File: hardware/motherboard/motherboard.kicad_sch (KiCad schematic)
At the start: 78 parts, among them J1 JST-VH, J2 USB C 2.0, J3 JST-VH, J4 JST-PH, Q1 TSM7P06CP_ROG, Q2 TSM7P06CP_ROG, SW1 Boot, SW10 B, SW11 X, SW12 Y, SW13 Start, SW14 Select, SW2 Reset, SW3 A, SW4 B, SW5 LB, SW6 RB, SW7 X, SW8 Y, SW9 A, U1 ESP32-S3-WROOM-1, U2 TPS75533KTTRG3, U3 TLV75709PDBV

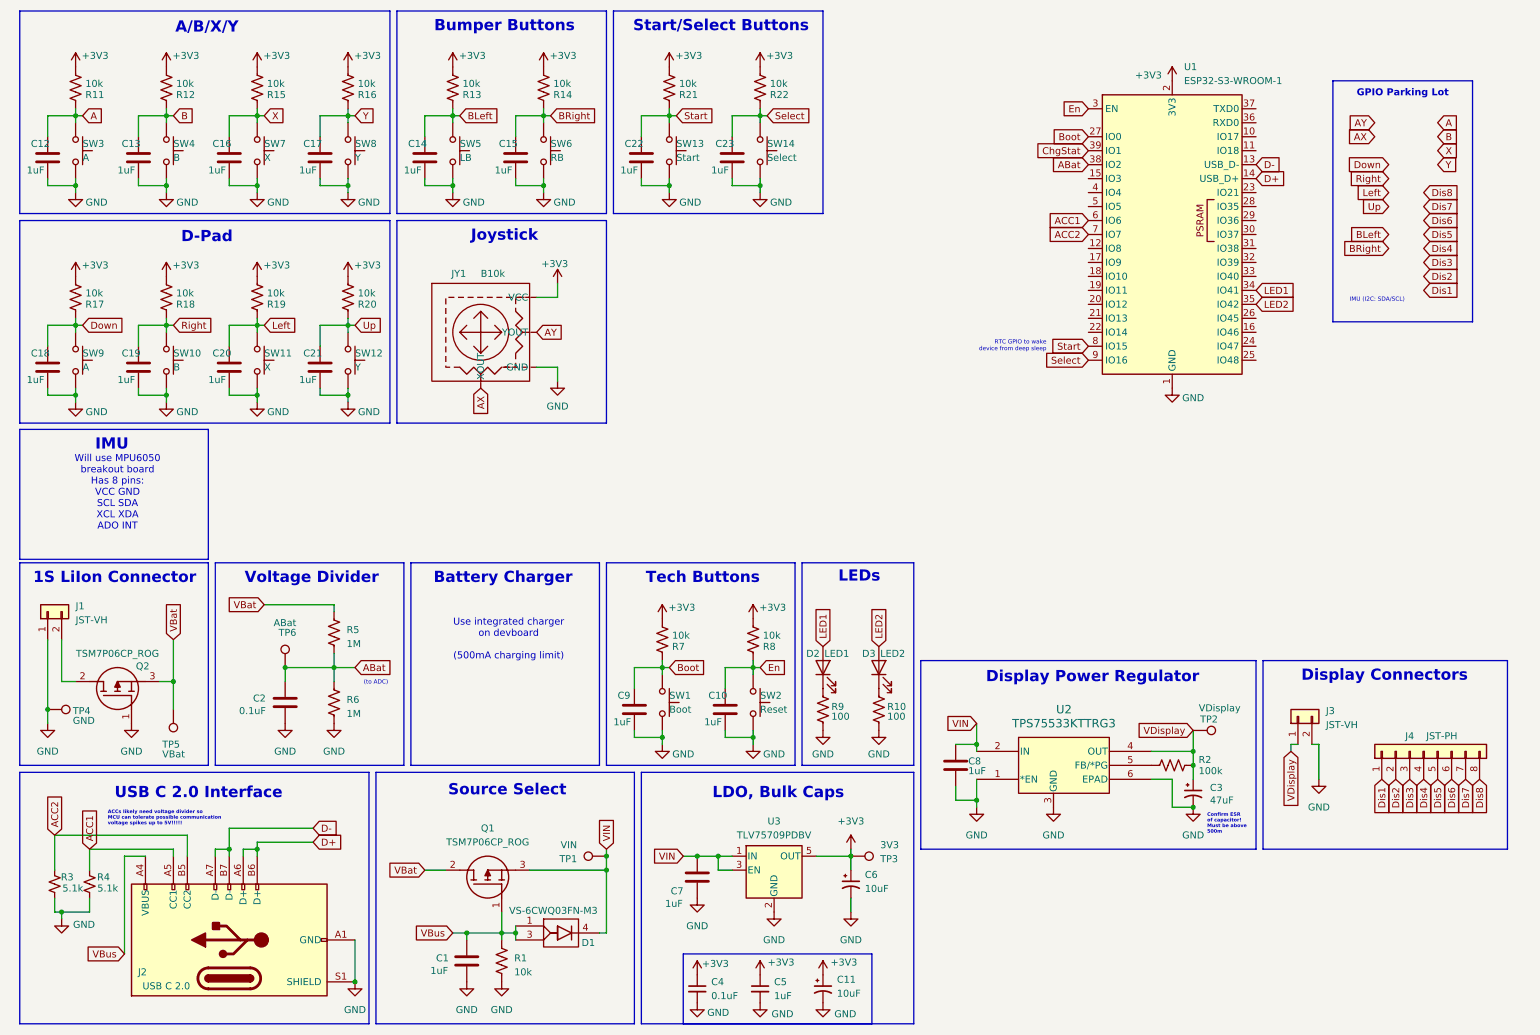
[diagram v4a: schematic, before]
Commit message: Charger, Started GPIO Assignments
Added ESP32 devboard charger circuit and began assigning GPIOs. Provided lots of annotations and justifications for GPIO assignments.
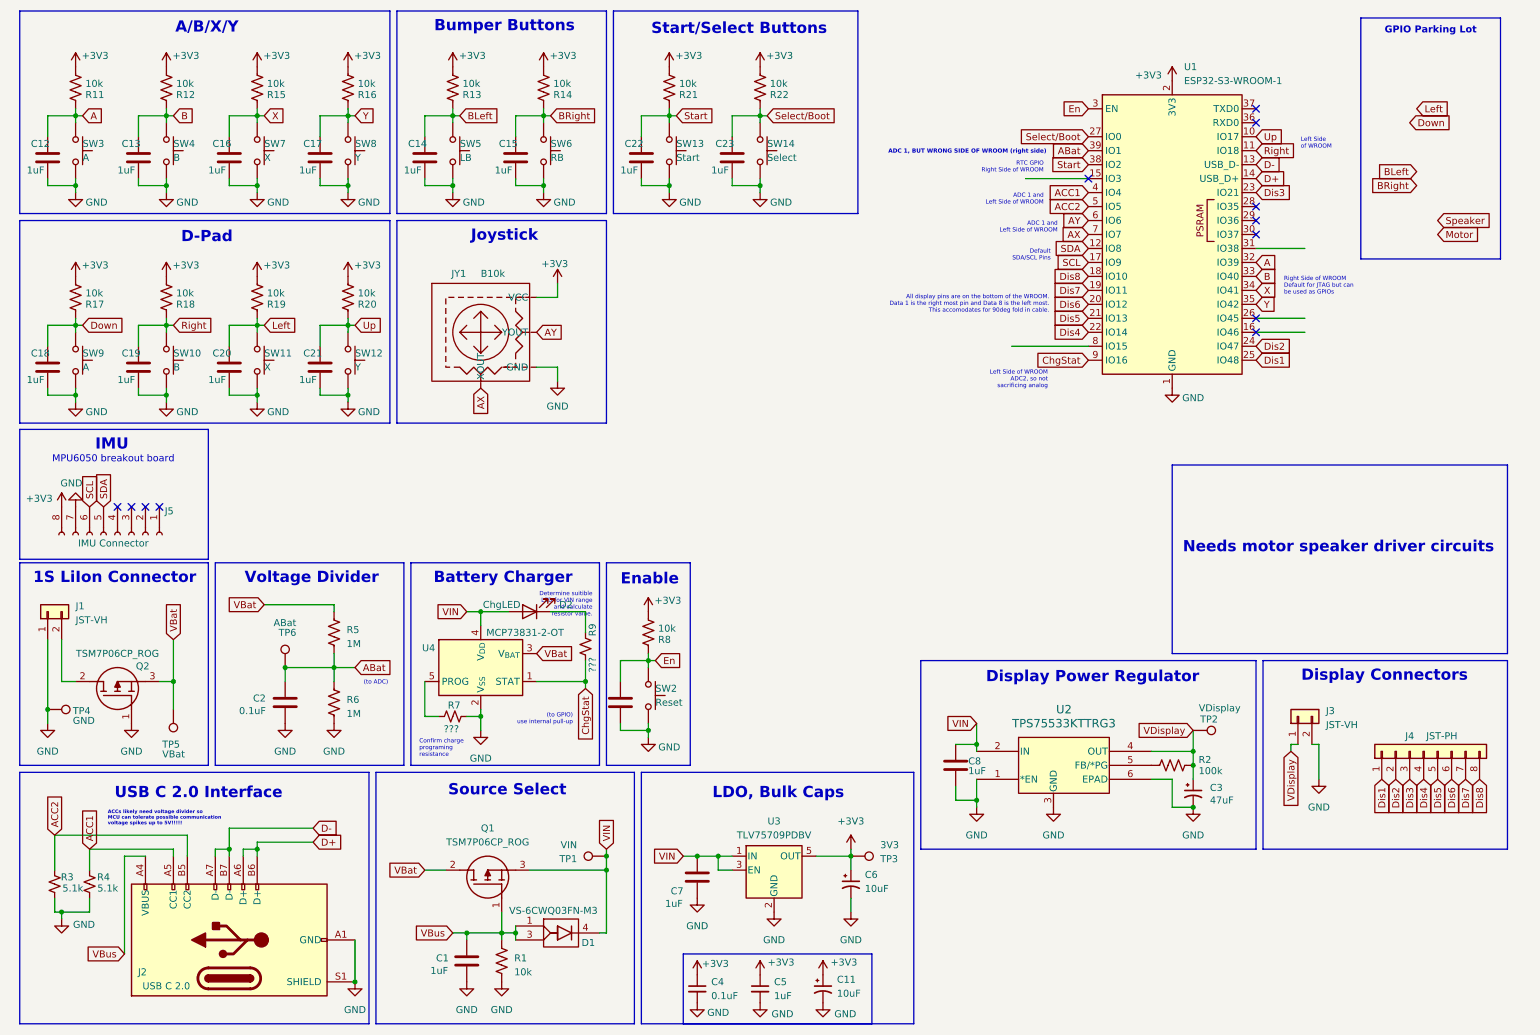
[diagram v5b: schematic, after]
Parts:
- removed C9: 1uF, symbol Device:C
- removed D3: LED2, symbol Device:LED
- removed R10, R9: 100, Resistor_SMD:R_0603_1608Metric, symbol Device:R_US
- removed R7: 10k, Resistor_SMD:R_0603_1608Metric, symbol Device:R_US
- removed SW1: Boot, symbol Switch:SW_Push
- added J5: IMU Connector, symbol Connector:Conn_01x08_Socket
- added R7, R9: ???, symbol Device:R_Small_US
- added U4: MCP73831-2-OT, Package_TO_SOT_SMD:SOT-23-5, symbol Battery_Management:MCP73831-2-OT
- D2: value LED1 -> ChgLED
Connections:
- net LED2 is gone; now on net Y: U1.35 (IO42)
- net +3V3: now also J5.8 (Pin_8)
- net A: now also U1.32 (IO39)
- net ABat: now also U1.39 (IO1); no longer U1.38 (IO2)
- net ACC1: now also U1.4 (IO4); no longer U1.6 (IO6)
- net ACC2: now also U1.5 (IO5); no longer U1.7 (IO7)
- net AX: now also U1.7 (IO7)
- net AY: now also U1.6 (IO6)
- net B: now also U1.33 (IO40)
- net ChgStat: now also U1.9 (IO16), R9.1, U4.1 (STAT); no longer U1.39 (IO1)
- net Dis1: now also U1.25 (IO48)
- net Dis2: now also U1.24 (IO47)
- net Dis3: now also U1.23 (IO21)
- net Dis4: now also U1.22 (IO14)
- net Dis5: now also U1.21 (IO13)
- net Dis6: now also U1.20 (IO12)
- net Dis7: now also U1.19 (IO11)
- net Dis8: now also U1.18 (IO10)
- net GND: now also J5.7 (Pin_7), R7.2, U4.2 (V_{SS})
- net Right: now also U1.11 (IO18)
- net Start: now also U1.38 (IO2); no longer U1.8 (IO15)
- net Up: now also U1.10 (IO17)
- net VBat: now also U4.3 (V_{BAT})
- net VIN: now also D2.2 (A), U4.4 (V_{DD})
- net X: now also U1.34 (IO41)
- net at D2.1 (K): now also R9.2
- net SDA: now reaches U1.12 (IO8)
- net SDA: now also J5.5 (Pin_5)
- net SCL: now reaches U1.17 (IO9)
- net SCL: now also J5.6 (Pin_6)
- net Boot renamed Select/Boot
- net Select/Boot: now also C23.1, R22.1, SW14.1
- removed net LED1: D2.2 (A), U1.34 (IO41)
- removed net Select: C23.1, R22.1, SW14.1, U1.9 (IO16)
- new net: R7.1, U4.5 (PROG)
- no-connect marks 0 -> 12
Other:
- note added: "(to GPIO) use internal pull-up"
- note added: "ADC 1 and Left Side of WROOM"
- note added: "ADC 1, BUT WRONG SIDE OF WROOM (right side)"
- note added: "All display pins are on the bottom of the WROOM. Data 1 is the right most pin and Data 8 is the left most. This accomodates for 90deg fold in cable."
- note added: "Confirm charge programing resistance"
- note added: "Default SDA/SCL Pins"
- note added: "Determine suitible LED for VIN range and calculate resistor value."
- note added: "Enable"
- note added: "Left Side of WROOM"
- note added: "Left Side of WROOM ADC2, so not sacrificing analog"
- note added: "MPU6050 breakout board"
- note added: "Needs motor speaker driver circuits"
- note added: "RTC GPIO Right Side of WROOM"
- note added: "Right Side of WROOM Default for JTAG but can be used as GPIOs"
- note removed: "Confirm ESR of capacitor! Must be above 500m"
- note removed: "IMU (I2C: SDA/SCL)"
- note removed: "LEDs"
- note removed: "RTC GPIO to wake device from deep sleep"
- note removed: "Tech Buttons"
- note removed: "Use integrated charger on devboard (500mA charging limit)"
- note removed: "Will use MPU6050 breakout board Has 8 pins: VCC GND SCL SDA XCL XDA ADO INT"
- moved on the sheet: R8, SW2

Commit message: Motherboard Minor Annotation Updates
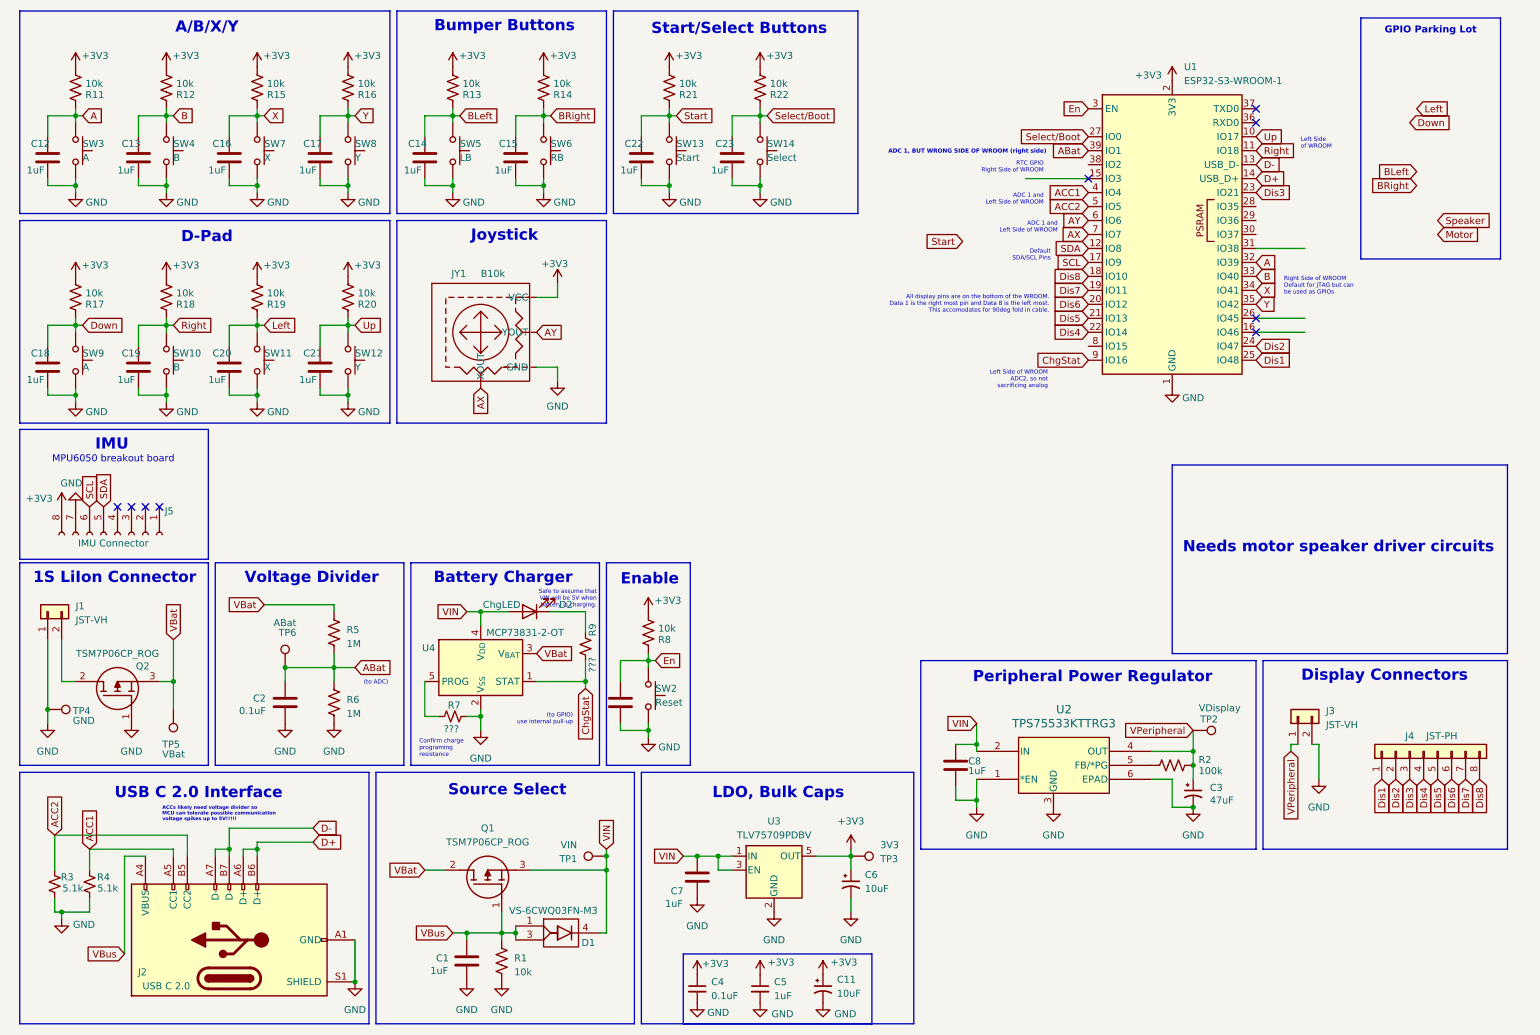
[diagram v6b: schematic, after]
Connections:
- net Start: no longer U1.38 (IO2)
- net VDisplay renamed VPeripheral
- no-connect marks 12 -> 9
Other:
- note added: "Peripheral Power Regulator"
- note added: "Safe to assume that VIN will be 5V when battery is charging."
- note removed: "Determine suitible LED for VIN range and calculate resistor value."
- note removed: "Display Power Regulator"
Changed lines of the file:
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@@
 		)
 	)
-	(text "Display Power Regulator"
+	(text "Peripheral Power Regulator"
 		(exclude_from_sim no)
 		(at 207.772 133.858 0)
@@
 		)
 	)
-	(text "Determine suitible\nLED for VIN range\nand calculate\nresistor value."
+	(text "Safe to assume that\nVIN will be 5V when\nbattery is charging."
 		(exclude_from_sim no)
-		(at 116.84 120.65 0)
+		(at 117.602 119.634 0)
 		(effects
 			(font
@@
 	(text "ACCs likely need voltage divider so\nMCU can tolerate possible communication \nvoltage spikes up to 5V!!!!!"
 		(exclude_from_sim no)
-		(at 28.702 159.512 0)
+		(at 38.608 158.75 0)
 		(effects
 			(font
@@
 	)
 	(no_connect
-		(at 237.49 48.26)
-	)
-	(no_connect
-		(at 237.49 50.8)
-	)
-	(no_connect
 		(at 33.02 102.87)
 	)
@@
 	)
 	(no_connect
-		(at 237.49 53.34)
-	)
-	(no_connect
 		(at 237.49 30.48)
 	)
@@
 	(wire
 		(pts
-			(xy 193.04 73.66) (xy 207.01 73.66)
-		)
-		(stroke
-			(width 0)
-			(type default)
-		)
-	)
-	(wire
-		(pts
 			(xy 39.37 69.85) (xy 39.37 68.58)
 		)
@@
 		)
 	)
-	(global_label "VDisplay"
+	(global_label "VPeripheral"
 		(shape input)
 		(at 243.84 147.32 270)
@@
 		)
 		(property "Intersheetrefs" "${INTERSHEET_REFS}"
-			(at 243.84 158.2275 90)
+			(at 243.84 161.1304 90)
 			(effects
 				(font
@@
 	(global_label "Start"
 		(shape input)
-		(at 207.01 40.64 180)
+		(at 184.15 54.61 180)
 		(fields_autoplaced yes)
 		(effects
@@
 		)
 		(property "Intersheetrefs" "${INTERSHEET_REFS}"
-			(at 199.4287 40.64 0)
+			(at 176.5687 54.61 0)
 			(effects
 				(font
@@
 		)
 	)
-	(global_label "VDisplay"
+	(global_label "VPeripheral"
 		(shape input)
 		(at 226.06 143.51 180)
@@
 		)
 		(property "Intersheetrefs" "${INTERSHEET_REFS}"
-			(at 215.1525 143.51 0)
+			(at 212.2496 143.51 0)
 			(effects
 				(font

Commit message: Added CC Voltage Divider and Updated Charge LED Resistor
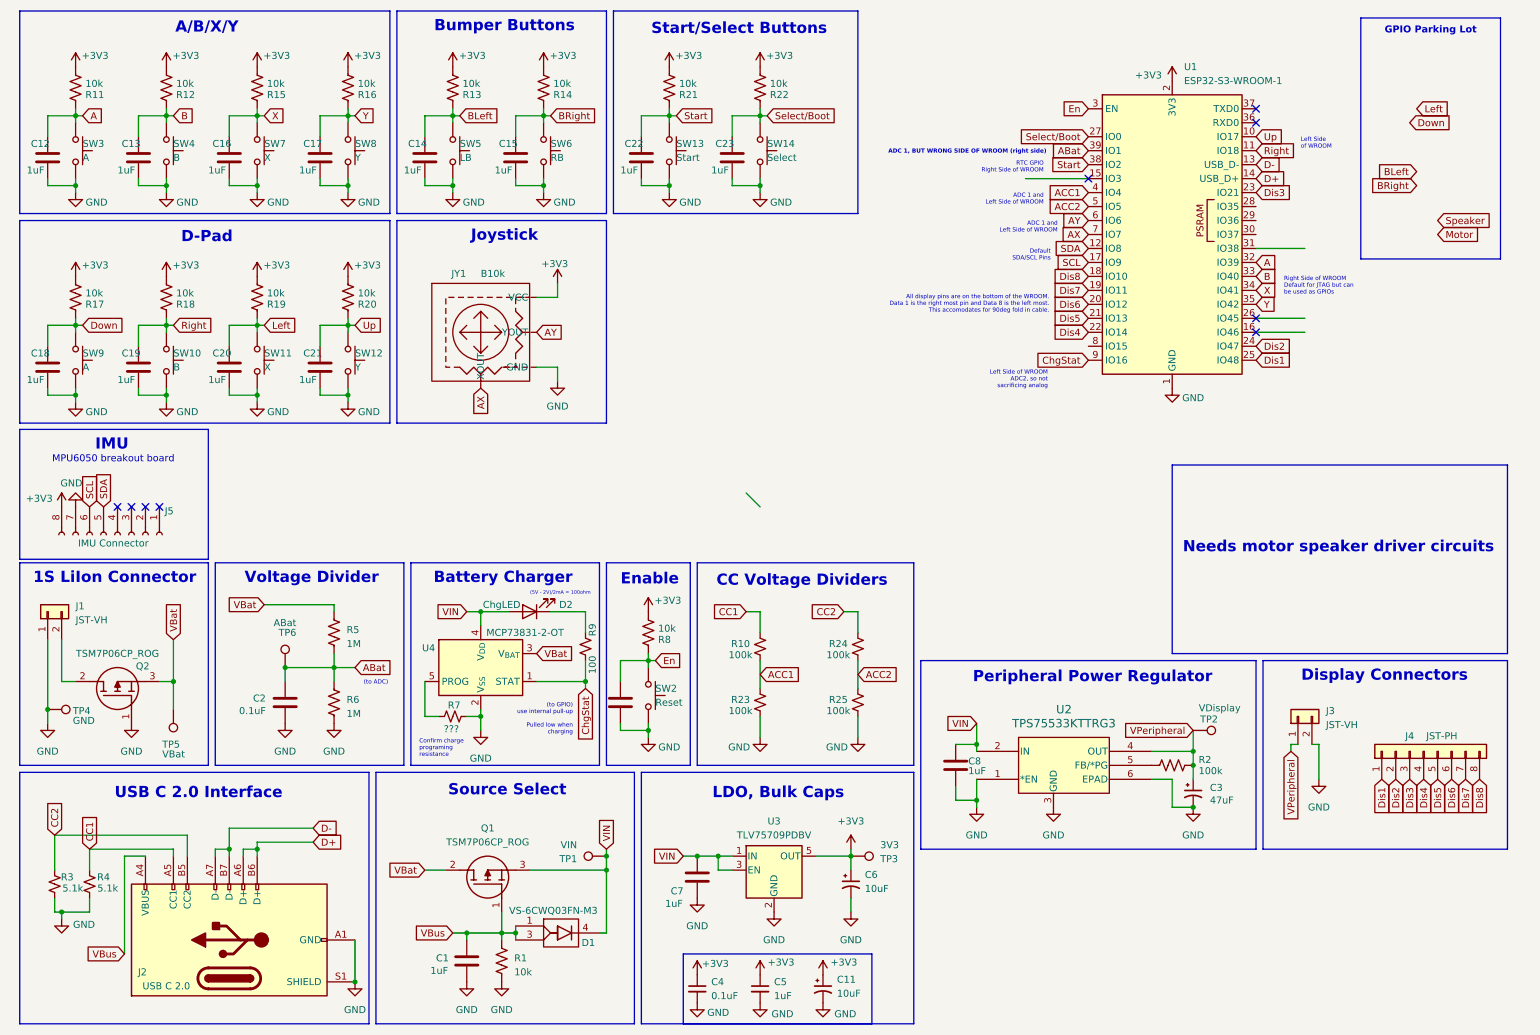
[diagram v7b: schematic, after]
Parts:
- added R10, R23, R24, R25: 100k, symbol Device:R_Small_US
- D2: footprint (none) -> LED_SMD:LED_1206_3216Metric
- R9: value ??? -> 100
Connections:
- net ACC1: now also R10.1, R23.2; no longer J2.A5 (CC1), R4.2
- net ACC2: now also R24.1, R25.2; no longer J2.B5 (CC2), R3.2
- net GND: now also R23.1, R25.1
- net Start: now also U1.38 (IO2)
- new net CC1: J2.A5 (CC1), R10.2, R4.2
- new net CC2: J2.B5 (CC2), R24.2, R3.2
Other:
- note added: "(5V - 2V)/2mA = 100ohm"
- note added: "(to GPIO) use internal pull-up Pulled low when charging"
- note added: "CC Voltage Dividers"
- note removed: "(to GPIO) use internal pull-up"
- note removed: "ACCs likely need voltage divider so MCU can tolerate possible communication voltage spikes up to 5V!!!!!"
- note removed: "Safe to assume that VIN will be 5V when battery is charging."
